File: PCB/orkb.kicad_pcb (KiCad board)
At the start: 2 copper layers, 148.5 x 113.3 mm, 109 parts, among them J1 USB_C_Receptacle_USB2.0, P1 OLED, SW1 MXHS, SW10 MXHS, SW11 MXHS, SW12 MXHS, SW13 MXHS, SW14 MXHS, SW15 MXHS, SW16 MXHS, SW17 MXHS, SW18 MXHS, SW19 MXHS, SW2 MXHS, SW20 MXHS, SW21 MXHS, SW22 MXHS, SW23 MXHS, SW24 MSK12C02, SW25 MSK12C02, SW3 MXHS, SW4 MXHS, SW5 MXHS, SW6 MXHS, SW7 MXHS, SW8 MXHS, SW9 MXHS, U1 ProMicro, U2 SRV05-4, U3 SRV05-4

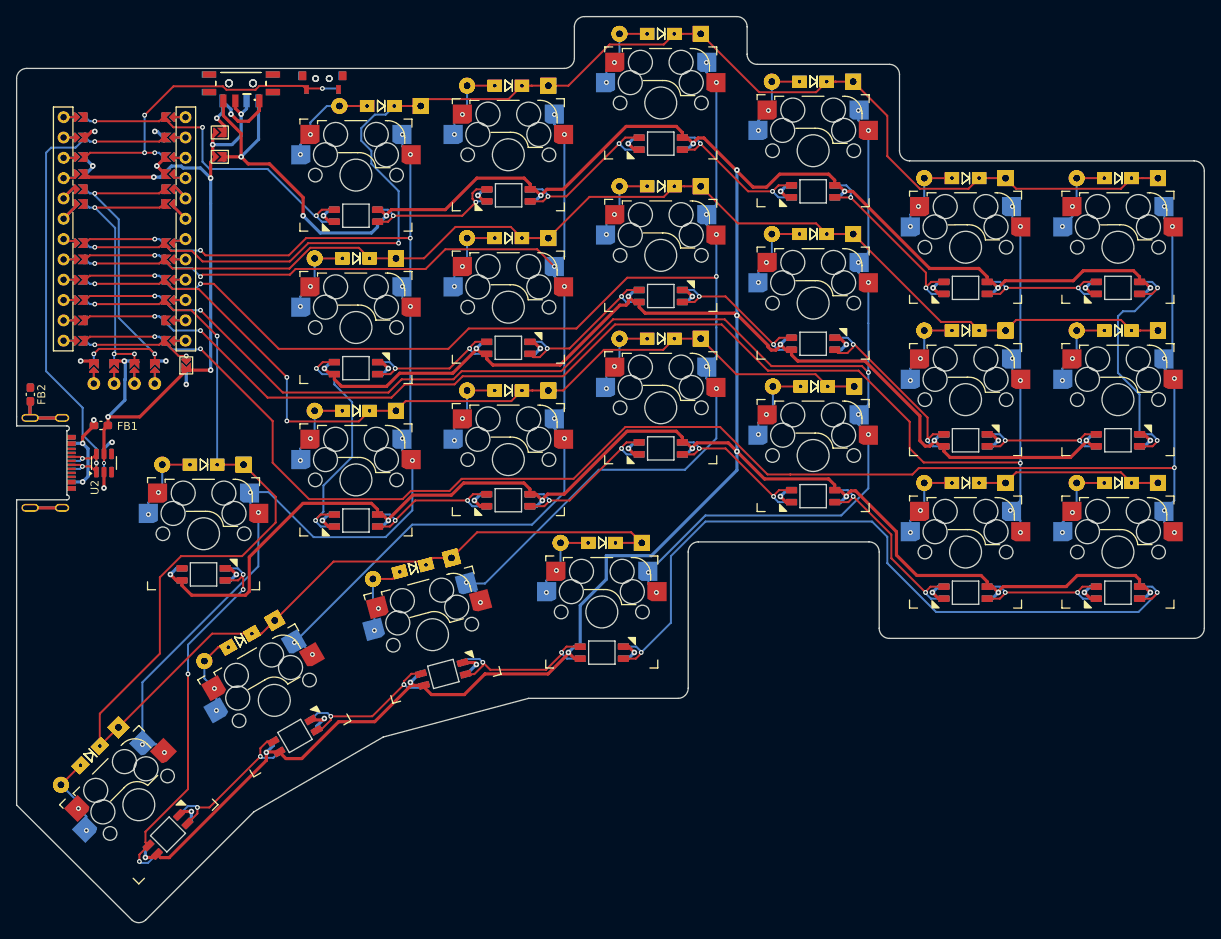
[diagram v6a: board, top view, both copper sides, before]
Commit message: Fix column routing for index/thumb cluster
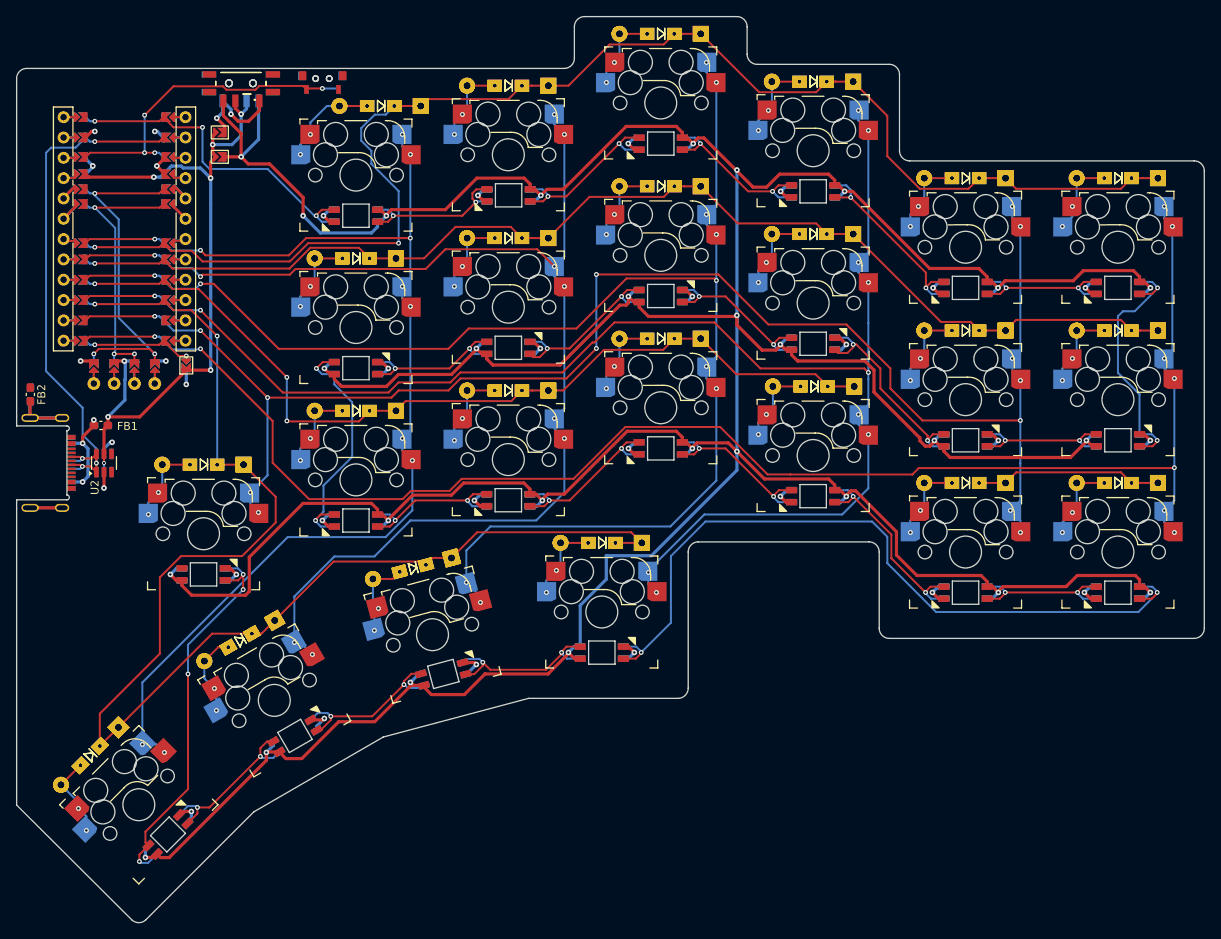
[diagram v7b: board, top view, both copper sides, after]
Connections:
- SW23 pad 1: col0 -> col4
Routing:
- net col4: track 177.2 -> 200.8 mm, vias 9 -> 14
- net col0: track 156.8 -> 145.3 mm, vias 13 -> 11
- net col2: track 178.7 -> 184.0 mm
- net col1: track 156.4 -> 159.8 mm
- net /PWR_KEY: track 610.0 -> 610.7 mm
